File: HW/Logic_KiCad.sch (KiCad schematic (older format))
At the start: 8 parts

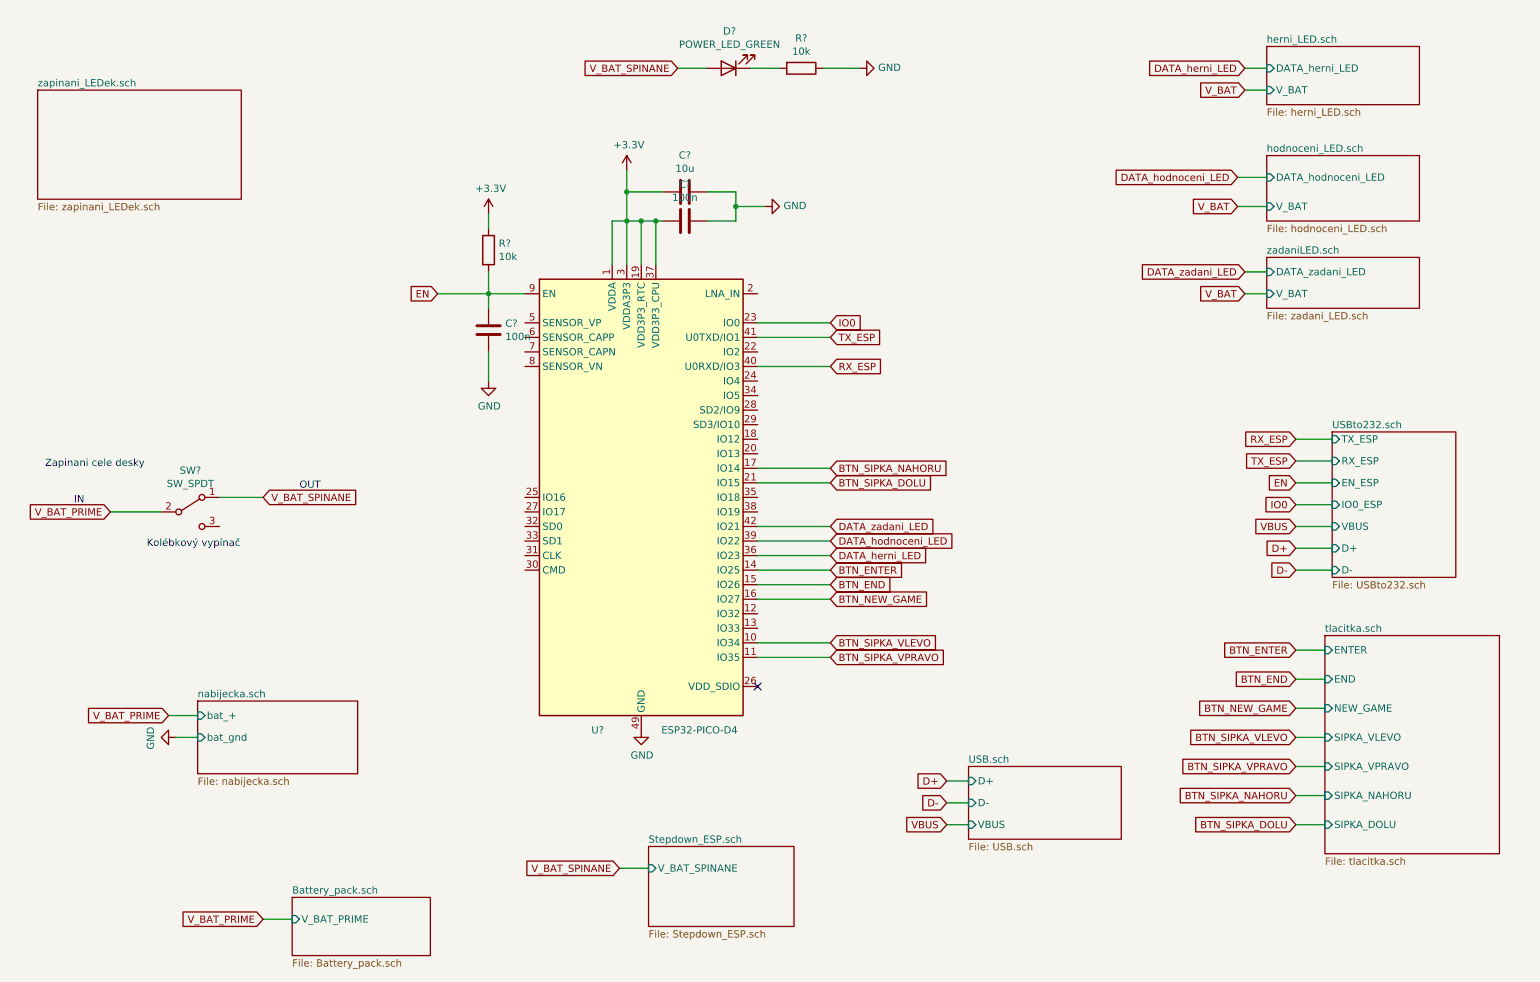
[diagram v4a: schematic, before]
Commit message: change structure of LEDs, add switching power supply of LEDs in parts
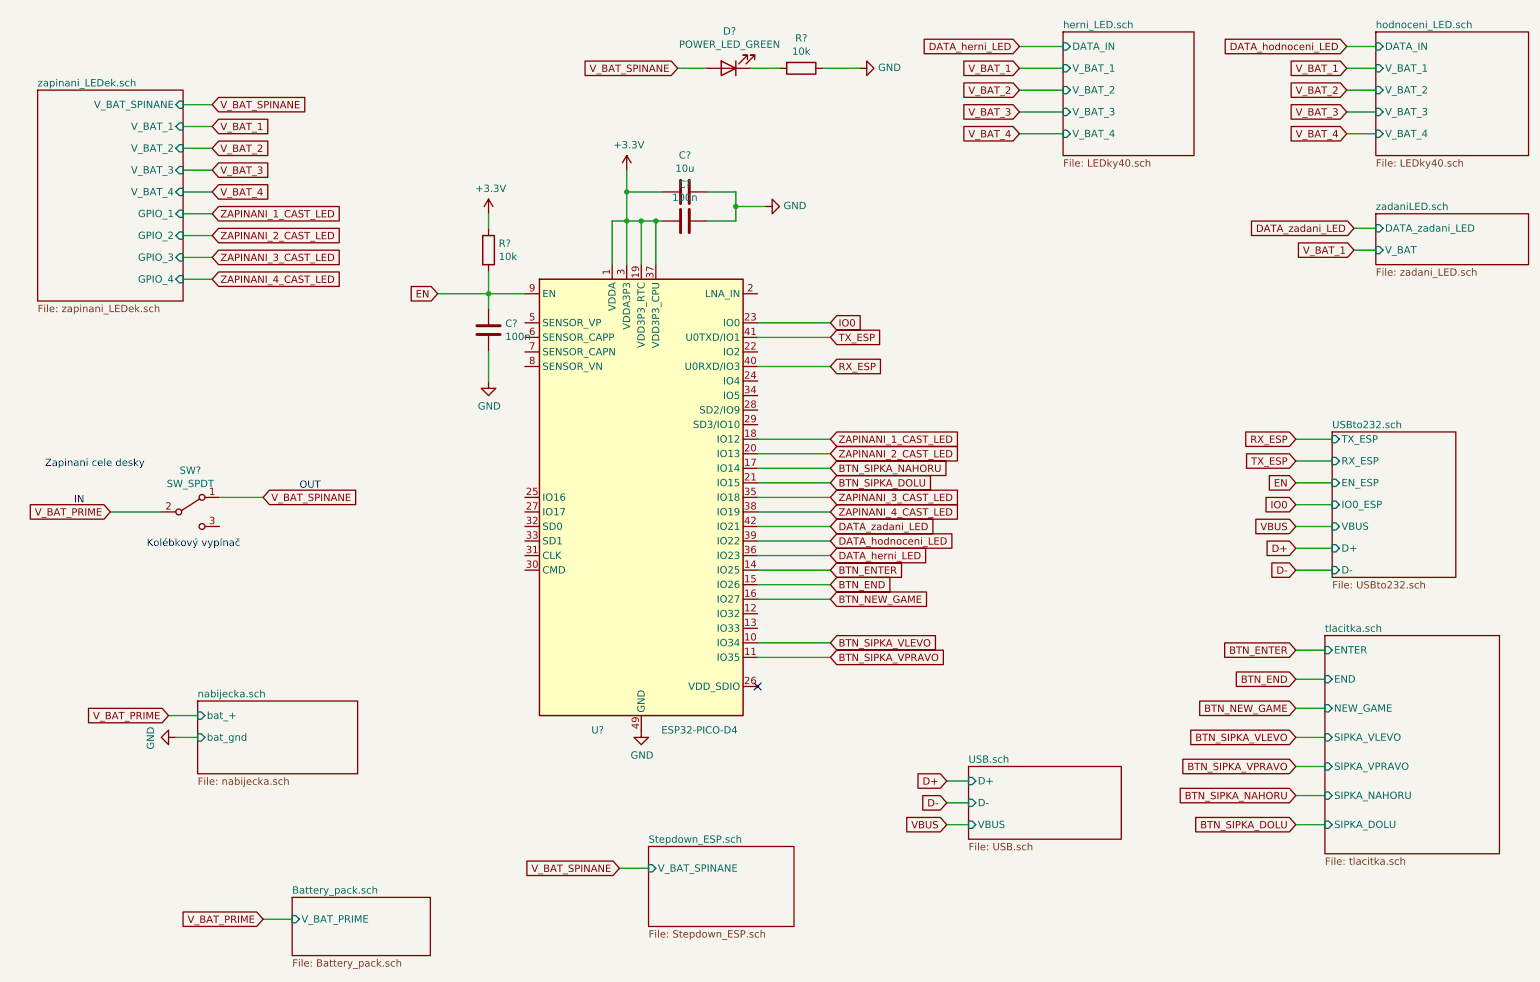
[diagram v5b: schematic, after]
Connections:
- net ZAPINANI_1_CAST_LED: now reaches U?.18 (IO12)
- net ZAPINANI_2_CAST_LED: now reaches U?.20 (IO13)
- net ZAPINANI_3_CAST_LED: now reaches U?.35 (IO18)
- net ZAPINANI_4_CAST_LED: now reaches U?.38 (IO19)
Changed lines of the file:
@@
 $Descr A4 11693 8268
 encoding utf-8
-Sheet 1 22
+Sheet 1 42
 Title ""
 Date ""
@@
 Comment4 ""
 $EndDescr
-$Sheet
-S 9200 750  1050 400
-U 5F70D6B6
-F0 "herni_LED.sch" 50
-F1 "herni_LED.sch" 50
-F2 "DATA_herni_LED" I L 9200 900 50
-F3 "V_BAT" I L 9200 1050 50
-$EndSheet
-Text GLabel 9050 900  0    50   Input ~ 0
+Text GLabel 7500 750  0    50   Input ~ 0
 DATA_herni_LED
-Wire Wire Line
-	9050 900  9200 900
-$Sheet
-S 9200 1500 1050 450
-U 5FACC290
-F0 "hodnoceni_LED.sch" 50
-F1 "hodnoceni_LED.sch" 50
-F2 "DATA_hodnoceni_LED" I L 9200 1650 50
-F3 "V_BAT" I L 9200 1850 50
-$EndSheet
-Text GLabel 9000 1650 0    50   Input ~ 0
+Text GLabel 9750 750  0    50   Input ~ 0
 DATA_hodnoceni_LED
 Wire Wire Line
-	9200 1650 9000 1650
-$Sheet
-S 9200 2200 1050 350
+	9950 750  9750 750
+$Sheet
+S 9950 1900 1050 350
 U 5FB682DC
 F0 "zadaniLED.sch" 50
 F1 "zadani_LED.sch" 50
-F2 "DATA_zadani_LED" I L 9200 2300 50
-F3 "V_BAT" I L 9200 2450 50
-$EndSheet
-Text GLabel 9050 2300 0    50   Input ~ 0
+F2 "DATA_zadani_LED" I L 9950 2000 50
+F3 "V_BAT" I L 9950 2150 50
+$EndSheet
+Text GLabel 9800 2000 0    50   Input ~ 0
 DATA_zadani_LED
 Wire Wire Line
-	9050 2300 9200 2300
+	9800 2000 9950 2000
 $Sheet
 S 9600 4800 1200 1500
@@
 Wire Wire Line
 	6150 900  6400 900
-Text GLabel 9050 1050 0    50   Input ~ 0
-V_BAT
-Text GLabel 9000 1850 0    50   Input ~ 0
-V_BAT
-Text GLabel 9050 2450 0    50   Input ~ 0
-V_BAT
-Wire Wire Line
-	9200 2450 9050 2450
-Wire Wire Line
-	9000 1850 9200 1850
-Wire Wire Line
-	9050 1050 9200 1050
+Text GLabel 9800 2150 0    50   Input ~ 0
+V_BAT_1
+Wire Wire Line
+	9950 2150 9800 2150
 $Sheet
 S 4950 6250 1000 550
@@
 	7000 6100 7150 6100
 $Sheet
-S 750  1050 1400 750
+S 750  1050 1000 1450
 U 5F7BA54B
 F0 "zapinani_LEDek.sch" 50
 F1 "zapinani_LEDek.sch" 50
-$EndSheet
+F2 "V_BAT_SPINANE" I R 1750 1150 50
+F3 "V_BAT_1" I R 1750 1300 50
+F4 "V_BAT_2" I R 1750 1450 50
+F5 "V_BAT_4" I R 1750 1750 50
+F6 "V_BAT_3" I R 1750 1600 50
+F7 "GPIO_1" I R 1750 1900 50
+F8 "GPIO_2" I R 1750 2050 50
+F9 "GPIO_3" I R 1750 2200 50
+F10 "GPIO_4" I R 1750 2350 50
+$EndSheet
+Text GLabel 1950 1150 2    50   Input ~ 0
+V_BAT_SPINANE
+Wire Wire Line
+	1750 1150 1950 1150
+Text GLabel 1950 1300 2    50   Input ~ 0
+V_BAT_1
+Text GLabel 1950 1450 2    50   Input ~ 0
+V_BAT_2
+Text GLabel 1950 1600 2    50   Input ~ 0
+V_BAT_3
+Text GLabel 1950 1750 2    50   Input ~ 0
+V_BAT_4
+Text GLabel 1950 1900 2    50   Input ~ 0
+ZAPINANI_1_CAST_LED
+Text GLabel 1950 2050 2    50   Input ~ 0
+ZAPINANI_2_CAST_LED
+Text GLabel 1950 2200 2    50   Input ~ 0
+ZAPINANI_3_CAST_LED
+Text GLabel 1950 2350 2    50   Input ~ 0
+ZAPINANI_4_CAST_LED
+Wire Wire Line
+	1950 1300 1750 1300
+Wire Wire Line
+	1750 1450 1950 1450
+Wire Wire Line
+	1950 1600 1750 1600
+Wire Wire Line
+	1750 1750 1950 1750
+Wire Wire Line
+	1950 1900 1750 1900
+Wire Wire Line
+	1750 2050 1950 2050
+Wire Wire Line
+	1950 2200 1750 2200
+Wire Wire Line
+	1750 2350 1950 2350
+$Sheet
+S 7800 650  900  850
+U 5F79BCD0
+F0 "herni_LED.sch" 50
+F1 "LEDky40.sch" 50
+F2 "V_BAT_1" I L 7800 900 50
+F3 "DATA_IN" I L 7800 750 50
+F4 "V_BAT_2" I L 7800 1050 50
+F5 "V_BAT_3" I L 7800 1200 50
+F6 "V_BAT_4" I L 7800 1350 50
+$EndSheet
+$Sheet
+S 9950 650  1050 850
+U 5FACC290
+F0 "hodnoceni_LED.sch" 50
+F1 "LEDky40.sch" 50
+F2 "V_BAT_1" I L 9950 900 50
+F3 "DATA_IN" I L 9950 750 50
+F4 "V_BAT_2" I L 9950 1050 50
+F5 "V_BAT_3" I L 9950 1200 50
+F6 "V_BAT_4" I L 9950 1350 50
+$EndSheet
+Text GLabel 9750 900  0    50   Input ~ 0
+V_BAT_1
+Text GLabel 9750 1050 0    50   Input ~ 0
+V_BAT_2
+Text GLabel 9750 1200 0    50   Input ~ 0
+V_BAT_3
+Text GLabel 9750 1350 0    50   Input ~ 0
+V_BAT_4
+Wire Wire Line
+	9750 900  9950 900
+Wire Wire Line
+	9750 1050 9950 1050
+Wire Wire Line
+	9750 1200 9950 1200
+Wire Wire Line
+	9950 1350 9750 1350
+Text GLabel 7500 900  0    50   Input ~ 0
+V_BAT_1
+Text GLabel 7500 1050 0    50   Input ~ 0
+V_BAT_2
+Text GLabel 7500 1200 0    50   Input ~ 0
+V_BAT_3
+Text GLabel 7500 1350 0    50   Input ~ 0
+V_BAT_4
+Wire Wire Line
+	7500 1350 7800 1350
+Wire Wire Line
+	7500 750  7800 750
+Wire Wire Line
+	7500 900  7800 900
+Wire Wire Line
+	7500 1050 7800 1050
+Wire Wire Line
+	7500 1200 7800 1200
+Text GLabel 6200 3450 2    50   Input ~ 0
+ZAPINANI_1_CAST_LED
+Text GLabel 6200 3550 2    50   Input ~ 0
+ZAPINANI_2_CAST_LED
+Text GLabel 6200 3850 2    50   Input ~ 0
+ZAPINANI_3_CAST_LED
+Text GLabel 6200 3950 2    50   Input ~ 0
+ZAPINANI_4_CAST_LED
+Wire Wire Line
+	6200 3450 5700 3450
+Wire Wire Line
+	6200 3550 5700 3550
+Wire Wire Line
+	5700 3850 6200 3850
+Wire Wire Line
+	5700 3950 6200 3950
 $EndSCHEMATC

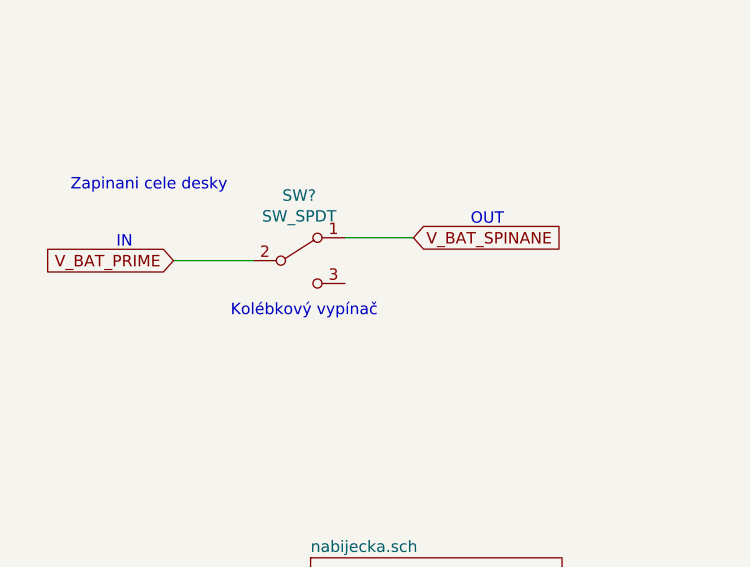
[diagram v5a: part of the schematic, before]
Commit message: remove pin from USB
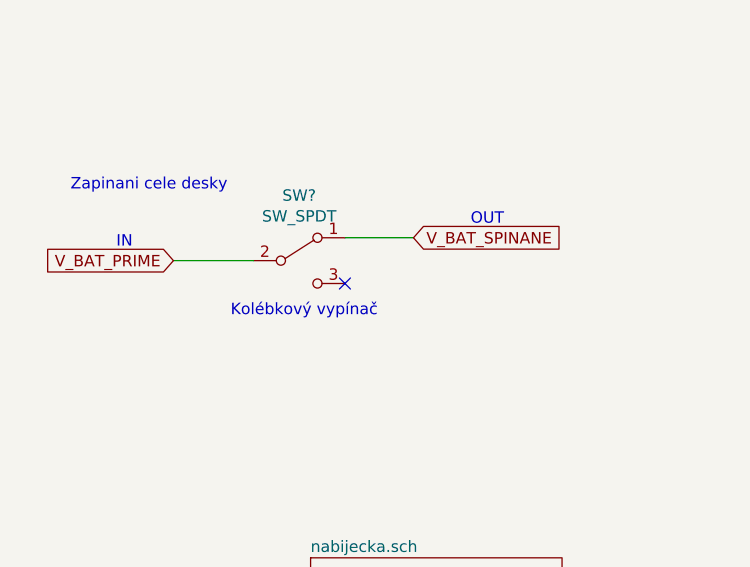
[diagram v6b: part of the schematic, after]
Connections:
- no-connect marks 1 -> 2
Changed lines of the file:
@@
 Wire Wire Line
 	5700 3950 6200 3950
+NoConn ~ 2000 4050
 $EndSCHEMATC

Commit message: add some packages
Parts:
- C?: footprint (none) -> Capacitor_SMD:C_1206_3216Metric
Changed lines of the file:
@@
 F 0 "C?" V 4948 1750 50  0000 C CNN
 F 1 "10u" V 5039 1750 50  0000 C CNN
-F 2 "" H 5238 1600 50  0001 C CNN
+F 2 "Capacitor_SMD:C_1206_3216Metric" H 5238 1600 50  0001 C CNN
 F 3 "~" H 5200 1750 50  0001 C CNN
 	1    5200 1750

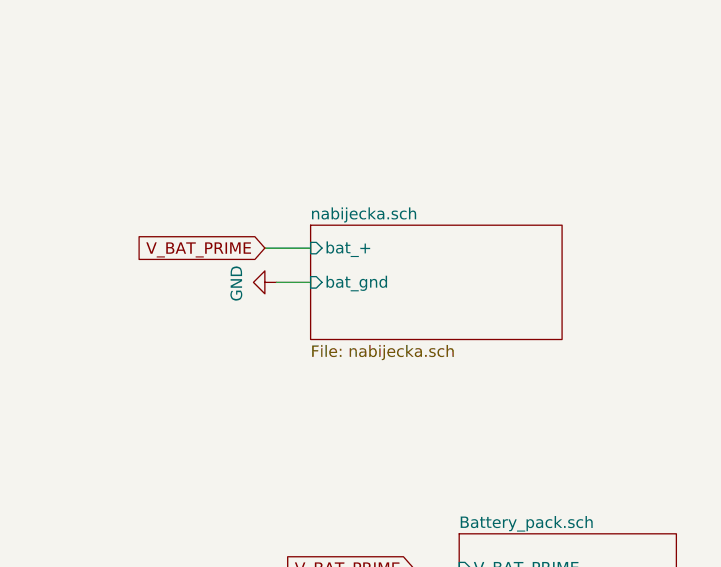
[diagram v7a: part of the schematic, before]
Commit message: add polyfuse for battery, remove resistor by SY8105, fix mistake by charger
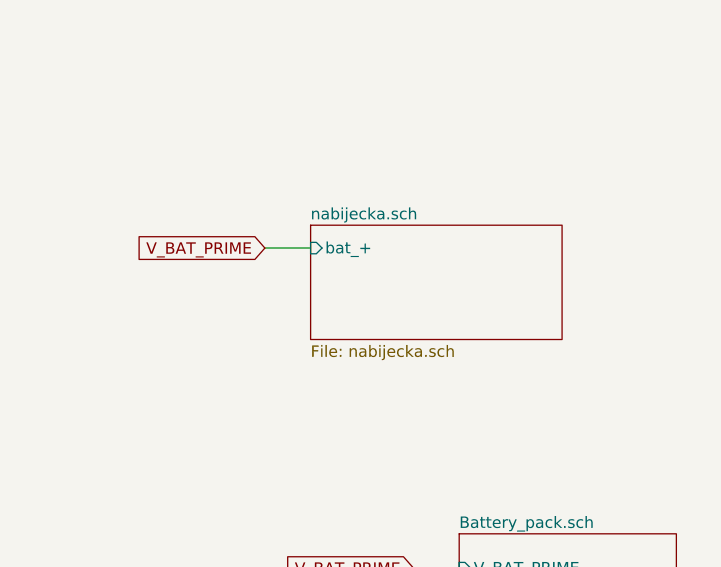
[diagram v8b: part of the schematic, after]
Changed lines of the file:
@@
 F1 "nabijecka.sch" 50
 F2 "bat_+" I L 1850 5350 50
-F3 "bat_gnd" I L 1850 5500 50
 $EndSheet
-$Comp
-L power:GND #PWR?
-U 1 1 5F73DAEF
-P 1700 5500
-F 0 "#PWR?" H 1700 5250 50  0001 C CNN
-F 1 "GND" H 1705 5327 50  0000 C CNN
-F 2 "" H 1700 5500 50  0001 C CNN
-F 3 "" H 1700 5500 50  0001 C CNN
-	1    1700 5500
-	0    1    1    0
-$EndComp
-Wire Wire Line
-	1700 5500 1850 5500
 Text GLabel 1650 5350 0    50   Input ~ 0
 V_BAT_PRIME
